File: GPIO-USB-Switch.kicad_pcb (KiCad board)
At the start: 2 copper layers, 20 x 38 mm, 16 parts, among them J1 Jetson_GPIO_OUT, J2 USB3.0-Type-A_Male, J3 USB3.0-Type-A_Female, Q1 BSS138, Q2 DMG2301L

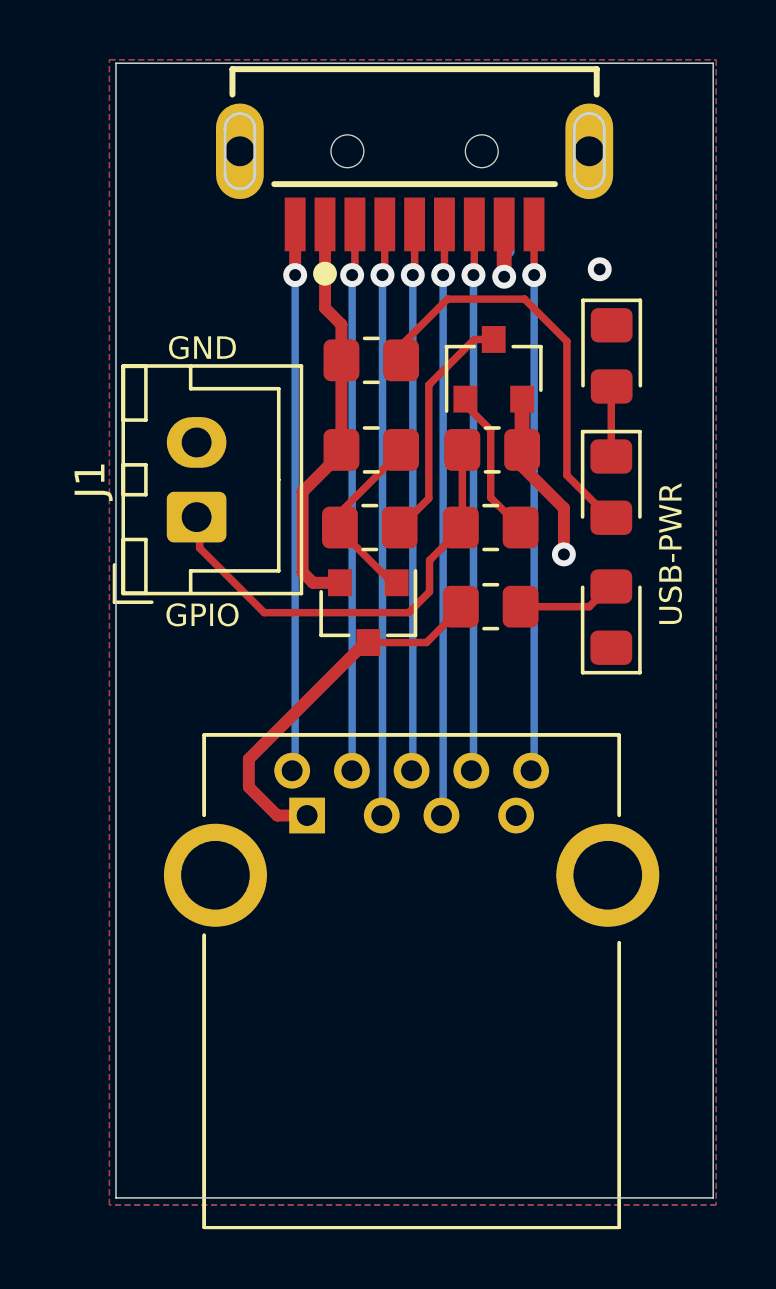
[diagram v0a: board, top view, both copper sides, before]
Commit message: added local labels for USB connectors
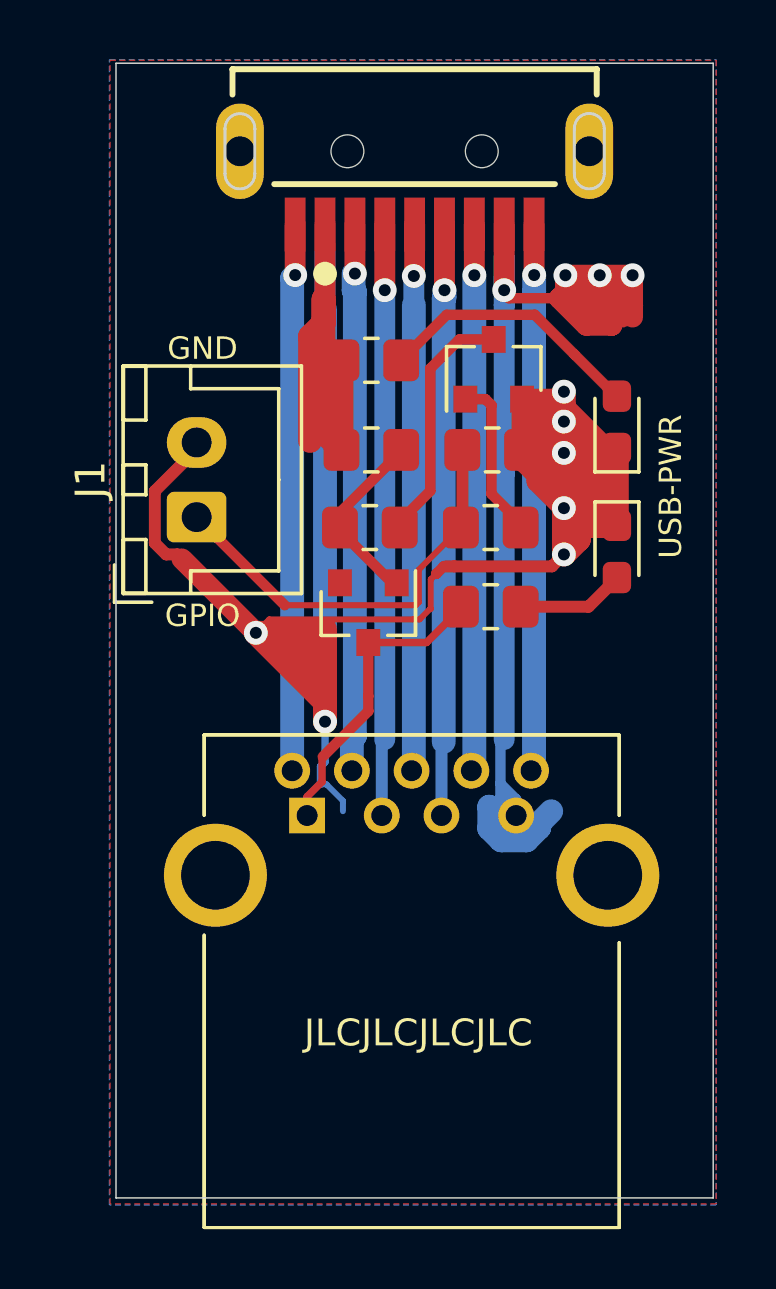
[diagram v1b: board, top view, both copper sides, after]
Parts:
- removed D1: D, Diode_SMD:D_0805_2012Metric_Pad1.15x1.40mm_HandSolder
- D2: value LED -> LED_Red; footprint LED_SMD:LED_0805_2012Metric_Pad1.15x1.40mm_HandSolder -> LED_SMD:LED_0603_1608Metric_Pad1.05x0.95mm_HandSolder
- D3: value LED -> LED_Green; footprint LED_SMD:LED_0805_2012Metric_Pad1.15x1.40mm_HandSolder -> LED_SMD:LED_0603_1608Metric_Pad1.05x0.95mm_HandSolder
- Q1: value BSS138 -> 2N7002
- moved D3 2.21 mm to (161.8, 88.3), turned to 270 degrees
- moved D2 2.18 mm to (161.8, 84.0), turned to 90 degrees
- moved G*** 1.62 mm to (149.8, 107.0)
- moved G*** 1.59 mm to (158.0, 107.0)
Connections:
- net Net-(J2-Pad1) renamed /VBUS
- net Net-(J2-Pad2) renamed /D-
- net Net-(J2-Pad3) renamed /D+
- net Net-(J2-Pad5) renamed /StdA_SSRX−
- net Net-(J2-Pad6) renamed /StdA_SSRX+
- net Net-(J2-Pad8) renamed /StdA_SSTX−
- net Net-(J2-Pad9) renamed /StdA_SSTX+
- D2 pad 1: Net-(D1-Pad2) -> GND
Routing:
- net GND: track 8.54 -> 138.5 mm, vias 3 -> 11
- net Net-(D2-Pad2): track 13.8 -> 9.14 mm
- net Net-(D1-Pad2): track 2.36 -> 0.00 mm
- net Net-(J3-Pad1): track 12.6 -> 10.4 mm
- net /VBUS: track 13.6 -> 15.4 mm
- net Net-(J1-Pad1): track 15.0 -> 14.4 mm
- net Net-(Q1-Pad1): track 5.12 -> 5.72 mm
- added copper zone on F.Cu, net /VBUS
- removed copper zone on F.Cu, net GND
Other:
- board text added: "JLCJLCJLCJLC"

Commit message: finished 4-layer layout!
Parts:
- D2, D3: footprint LED_SMD:LED_0603_1608Metric_Pad1.05x0.95mm_HandSolder -> LED_SMD:LED_0603_1608Metric
- J1: value Jetson_GPIO_OUT -> GPIO_OUT
- R1, R2, R3, R4, R5, R6: footprint Resistor_SMD:R_0805_2012Metric_Pad1.20x1.40mm_HandSolder -> Resistor_SMD:R_0603_1608Metric
- moved J1 13.4 mm to (161.1, 87.7)
- moved Q1 11.5 mm to (149.7, 90.5), turned to 180 degrees
- moved Q2 8.43 mm to (149.6, 82.9), turned to 180 degrees
- moved D2 8.40 mm to (153.4, 82.9), turned to 270 degrees
- moved D3 7.58 mm to (156.5, 82.9)
- moved R1 5.56 mm to (156.5, 90.4), turned to 90 degrees
- moved R2 4.99 mm to (153.4, 90.4), turned to 270 degrees
- moved R3 4.88 mm to (148.7, 86.7), turned to 90 degrees
- moved R4 4.70 mm to (153.4, 86.7), turned to 270 degrees
- moved R6 3.70 mm to (156.5, 86.7), turned to 90 degrees
- moved R5 3.40 mm to (150.6, 86.7), turned to 270 degrees
- moved J3 0.10 mm to (151.5, 97.2)
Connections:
- net /D+ renamed D+
- net /D- renamed D-
- net /StdA_SSRX+ renamed StdA_SSRX+
- net /StdA_SSRX− renamed StdA_SSRX-
- net /StdA_SSTX+ renamed StdA_SSTX+
- net /StdA_SSTX− renamed StdA_SSTX-
- net /VBUS renamed VBUS
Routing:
- net GND: track 138.5 -> 15.5 mm, vias 11 -> 44
- net Net-(J3-Pad1): track 10.4 -> 37.5 mm, vias 0 -> 3
- net Net-(D2-Pad2): track 9.14 -> 2.08 mm
- net Net-(J1-Pad1): track 14.4 -> 7.55 mm, vias 0 -> 1
- net Net-(Q1-Pad3): track 8.28 -> 2.92 mm, vias 0 -> 2
- net Net-(Q1-Pad1): track 5.72 -> 2.88 mm
- net VBUS: track 15.4 -> 18.0 mm, vias 0 -> 4
- net Net-(Q2-Pad1): track 5.74 -> 3.78 mm
- net Net-(D3-Pad2): track 3.72 -> 2.08 mm
- net D+: track 19.5 -> 20.3 mm
- added copper zone on F.Cu, net GND
- removed copper zone on F.Cu, net VBUS
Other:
- copper layers 2 -> 4
- rule via_min_drill: 0.3 -> 0.2
